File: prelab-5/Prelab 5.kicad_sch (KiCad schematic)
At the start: 8 parts, among them SW1 SW_Push, SW2 SW_DIP_x08, U1 74HC74

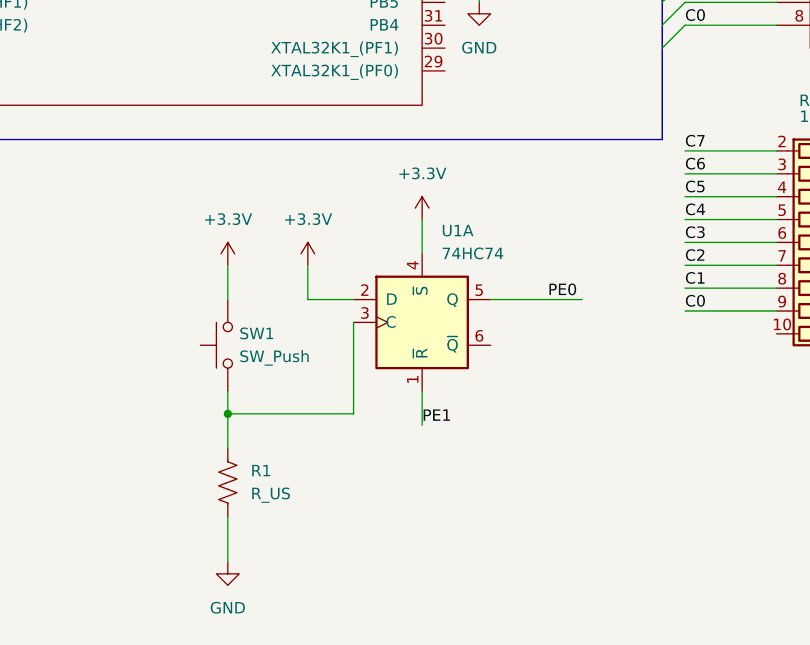
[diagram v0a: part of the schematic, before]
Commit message: Update Prelab title and added power pins to the flipflop
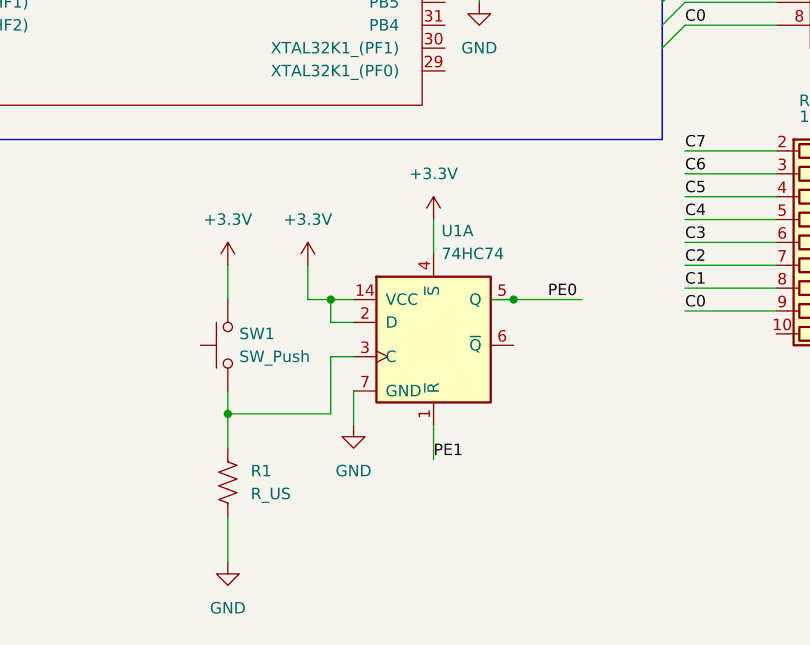
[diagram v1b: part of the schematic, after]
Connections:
- net +3.3V: now also U1.14 (VCC)
- net GND: now also U1.7 (GND)
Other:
- title: Lab 04 DIP switch and Bargraphs, Design task 1 -> Lab 05 Switch Debouncing, Polling, and Conditional I/O

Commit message: Added PE2 connection
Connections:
- net +3.3V: now also SW1.1; no longer SW1.2
- net GND: no longer B1.42 (GND)
- net PE2: now reaches R1.1, U1.3 (C)
- net PE2: now also B1.40 (PE2_(OP2_OUT)), SW1.2; no longer SW1.1
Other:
- moved on the sheet: R1, SW1
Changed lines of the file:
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@@
 	)
 	(junction
-		(at 97.79 144.78)
+		(at 97.79 138.43)
 		(diameter 0)
 		(color 0 0 0 0)
@@
 	)
 	(junction
+		(at 102.87 138.43)
+		(diameter 0)
+		(color 0 0 0 0)
+	)
+	(junction
 		(at 173.99 96.52)
 		(diameter 0)
@@
 	(wire
 		(pts
+			(xy 83.82 138.43) (xy 87.63 138.43)
+		)
+		(stroke
+			(width 0)
+			(type default)
+		)
+	)
+	(wire
+		(pts
 			(xy 43.18 86.36) (xy 57.15 86.36)
 		)
@@
 	(wire
 		(pts
-			(xy 97.79 128.27) (xy 97.79 132.08)
+			(xy 83.82 134.62) (xy 83.82 138.43)
 		)
 		(stroke
@@
 	(wire
 		(pts
-			(xy 121.92 73.66) (xy 124.46 73.66)
-		)
-		(stroke
-			(width 0)
-			(type default)
-		)
-	)
-	(wire
-		(pts
 			(xy 154.94 55.88) (xy 166.37 55.88)
 		)
@@
 	(wire
 		(pts
-			(xy 109.22 144.78) (xy 97.79 144.78)
+			(xy 97.79 138.43) (xy 102.87 138.43)
 		)
 		(stroke
@@
 	(wire
 		(pts
-			(xy 109.22 138.43) (xy 109.22 144.78)
-		)
-		(stroke
-			(width 0)
-			(type default)
-		)
-	)
-	(wire
-		(pts
 			(xy 154.94 48.26) (xy 166.37 48.26)
 		)
@@
 		)
 	)
-	(wire
-		(pts
-			(xy 124.46 73.66) (xy 124.46 74.93)
-		)
-		(stroke
-			(width 0)
-			(type default)
-		)
-	)
 	(bus
 		(pts
@@
 	(wire
 		(pts
+			(xy 102.87 138.43) (xy 102.87 143.51)
+		)
+		(stroke
+			(width 0)
+			(type default)
+		)
+	)
+	(wire
+		(pts
 			(xy 148.59 125.73) (xy 158.75 125.73)
 		)
@@
 	(wire
 		(pts
-			(xy 111.76 138.43) (xy 109.22 138.43)
+			(xy 102.87 138.43) (xy 111.76 138.43)
 		)
 		(stroke
@@
 	(wire
 		(pts
+			(xy 121.92 78.74) (xy 133.35 78.74)
+		)
+		(stroke
+			(width 0)
+			(type default)
+		)
+	)
+	(wire
+		(pts
 			(xy 125.73 96.52) (xy 125.73 99.06)
 		)
@@
 	(wire
 		(pts
-			(xy 97.79 156.21) (xy 97.79 161.29)
+			(xy 97.79 149.86) (xy 97.79 154.94)
 		)
 		(stroke
@@
 	(wire
 		(pts
-			(xy 97.79 142.24) (xy 97.79 144.78)
-		)
-		(stroke
-			(width 0)
-			(type default)
-		)
-	)
-	(wire
-		(pts
-			(xy 97.79 144.78) (xy 97.79 148.59)
+			(xy 97.79 138.43) (xy 97.79 142.24)
 		)
 		(stroke
@@
 		)
 	)
+	(label "PE2"
+		(at 102.87 143.51 90)
+		(effects
+			(font
+				(size 1.27 1.27)
+			)
+			(justify left bottom)
+		)
+	)
+	(label "PE2"
+		(at 129.54 78.74 0)
+		(effects
+			(font
+				(size 1.27 1.27)
+			)
+			(justify left bottom)
+		)
+	)
 	(label "C1"
 		(at 148.59 130.81 0)
@@
 	)
 	(symbol
-		(lib_id "power:GND")
-		(at 124.46 74.93 0)
-		(unit 1)
-		(body_style 1)
-		(exclude_from_sim no)
-		(in_bom yes)
-		(on_board yes)
-		(in_pos_files yes)
-		(dnp no)
-		(fields_autoplaced yes)
-		(property "Reference" "#PWR03"
-			(at 124.46 81.28 0)
-			(hide yes)
-			(show_name no)
-			(do_not_autoplace no)
-			(effects
-				(font
-					(size 1.27 1.27)
-				)
-			)
-		)
-		(property "Value" "GND"
-			(at 124.46 80.01 0)
-			(show_name no)
-			(do_not_autoplace no)
-			(effects
-				(font
-					(size 1.27 1.27)
-				)
-			)
-		)
-		(property "Footprint" ""
-			(at 124.46 74.93 0)
-			(hide yes)
-			(show_name no)
-			(do_not_autoplace no)
-			(effects
-				(font
-					(size 1.27 1.27)
-				)
-			)
-		)
-		(property "Datasheet" ""
-			(at 124.46 74.93 0)
-			(hide yes)
-			(show_name no)
-			(do_not_autoplace no)
-			(effects
-				(font
-					(size 1.27 1.27)
-				)
-			)
-		)
-		(property "Description" "Power symbol creates a global label with name \"GND\" , ground"
-			(at 124.46 74.93 0)
-			(hide yes)
-			(show_name no)
-			(do_not_autoplace no)
-			(effects
-				(font
-					(size 1.27 1.27)
-				)
-			)
-		)
-		(pin "1"
-		)
-		(instances
-			(project "Prelab 5"
-				(path "/b652f389-5275-44bd-a341-8481a2ee4dd0"
-					(reference "#PWR03")
-					(unit 1)
-				)
-			)
-		)
-	)
-	(symbol
 		(lib_id "power:+3.3V")
-		(at 97.79 128.27 0)
+		(at 83.82 134.62 0)
 		(unit 1)
 		(body_style 1)
@@
 		(fields_autoplaced yes)
 		(property "Reference" "#PWR08"
-			(at 97.79 132.08 0)
+			(at 83.82 138.43 0)
 			(hide yes)
 			(show_name no)
@@
 		)
 		(property "Value" "+3.3V"
-			(at 97.79 123.19 0)
+			(at 83.82 129.54 0)
 			(show_name no)
 			(do_not_autoplace no)
@@
 		)
 		(property "Footprint" ""
-			(at 97.79 128.27 0)
+			(at 83.82 134.62 0)
 			(hide yes)
 			(show_name no)
@@
 		)
 		(property "Datasheet" ""
-			(at 97.79 128.27 0)
+			(at 83.82 134.62 0)
 			(hide yes)
 			(show_name no)
@@
 		)
 		(property "Description" "Power symbol creates a global label with name \"+3.3V\""
-			(at 97.79 128.27 0)
+			(at 83.82 134.62 0)
 			(hide yes)
 			(show_name no)
@@
 	(symbol
 		(lib_id "Switch:SW_Push")
-		(at 97.79 137.16 90)
+		(at 92.71 138.43 0)
 		(unit 1)
 		(body_style 1)
@@
 		(fields_autoplaced yes)
 		(property "Reference" "SW1"
-			(at 99.06 135.8899 90)
-			(show_name no)
-			(do_not_autoplace no)
-			(effects
-				(font
-					(size 1.27 1.27)
-				)
-				(justify right)
+			(at 92.71 130.81 0)
+			(show_name no)
+			(do_not_autoplace no)
+			(effects
+				(font
+					(size 1.27 1.27)
+				)
 			)
 		)
 		(property "Value" "SW_Push"
-			(at 99.06 138.4299 90)
-			(show_name no)
-			(do_not_autoplace no)
-			(effects
-				(font
-					(size 1.27 1.27)
-				)
-				(justify right)
+			(at 92.71 133.35 0)
+			(show_name no)
+			(do_not_autoplace no)
+			(effects
+				(font
+					(size 1.27 1.27)
+				)
 			)
 		)
 		(property "Footprint" "Button_Switch_SMD:Nidec_Copal_CAS-120A"
-			(at 92.71 137.16 0)
+			(at 92.71 133.35 0)
 			(hide yes)
 			(show_name no)
@@
 		)
 		(property "Datasheet" ""
-			(at 92.71 137.16 0)
+			(at 92.71 133.35 0)
 			(hide yes)
 			(show_name no)
@@
 		)
 		(property "Description" "Push button switch, generic, two pins"
-			(at 97.79 137.16 0)
+			(at 92.71 138.43 0)
 			(hide yes)
 			(show_name no)
@@
 	(symbol
 		(lib_id "Device:R_US")
-		(at 97.79 152.4 0)
+		(at 97.79 146.05 0)
 		(unit 1)
 		(body_style 1)
@@
 		(in_pos_files yes)
 		(dnp no)
-		(fields_autoplaced yes)
 		(property "Reference" "R1"
-			(at 100.33 151.1299 0)
+			(at 90.424 144.526 0)
 			(show_name no)
 			(do_not_autoplace no)
@@
 		)
 		(property "Value" "R_US"
-			(at 100.33 153.6699 0)
+			(at 90.424 147.066 0)
 			(show_name no)
 			(do_not_autoplace no)
@@
 		)
 		(property "Footprint" "Package_DIP:DIP-8_W7.62mm"
-			(at 98.806 152.654 90)
+			(at 98.806 146.304 90)
 			(hide yes)
 			(show_name no)
@@
 		)
 		(property "Datasheet" ""
-			(at 97.79 152.4 0)
+			(at 97.79 146.05 0)
 			(hide yes)
 			(show_name no)
@@
 		)
 		(property "Description" "Resistor, US symbol"
-			(at 97.79 152.4 0)
+			(at 97.79 146.05 0)
 			(hide yes)
 			(show_name no)
@@
 	(symbol
 		(lib_id "power:GND")
-		(at 97.79 161.29 0)
+		(at 97.79 154.94 0)
 		(unit 1)
 		(body_style 1)
@@
 		(fields_autoplaced yes)
 		(property "Reference" "#PWR01"
-			(at 97.79 167.64 0)
+			(at 97.79 161.29 0)
 			(hide yes)
 			(show_name no)
@@
 		)
 		(property "Value" "GND"
-			(at 97.79 166.37 0)
+			(at 97.79 160.02 0)
 			(show_name no)
 			(do_not_autoplace no)
@@
 		)
 		(property "Footprint" ""
-			(at 97.79 161.29 0)
+			(at 97.79 154.94 0)
 			(hide yes)
 			(show_name no)
@@
 		)
 		(property "Datasheet" ""
-			(at 97.79 161.29 0)
+			(at 97.79 154.94 0)
 			(hide yes)
 			(show_name no)
@@
 		)
 		(property "Description" "Power symbol creates a global label with name \"GND\" , ground"
-			(at 97.79 161.29 0)
-			(hide yes)
-			(show_name no)
+			(at 97.79 154.94 0)
+			(hide yes)
+			(show_name no)
